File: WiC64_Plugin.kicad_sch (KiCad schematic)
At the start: 63 parts, among them CN1 PLUS4_USERPORT, CN2 OLED0.96, Q1 BSS138, Q10 BSS138, Q11 BSS138, Q2 BSS138, Q3 BSS138, Q4 BSS138, Q5 BSS138, Q6 BSS138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

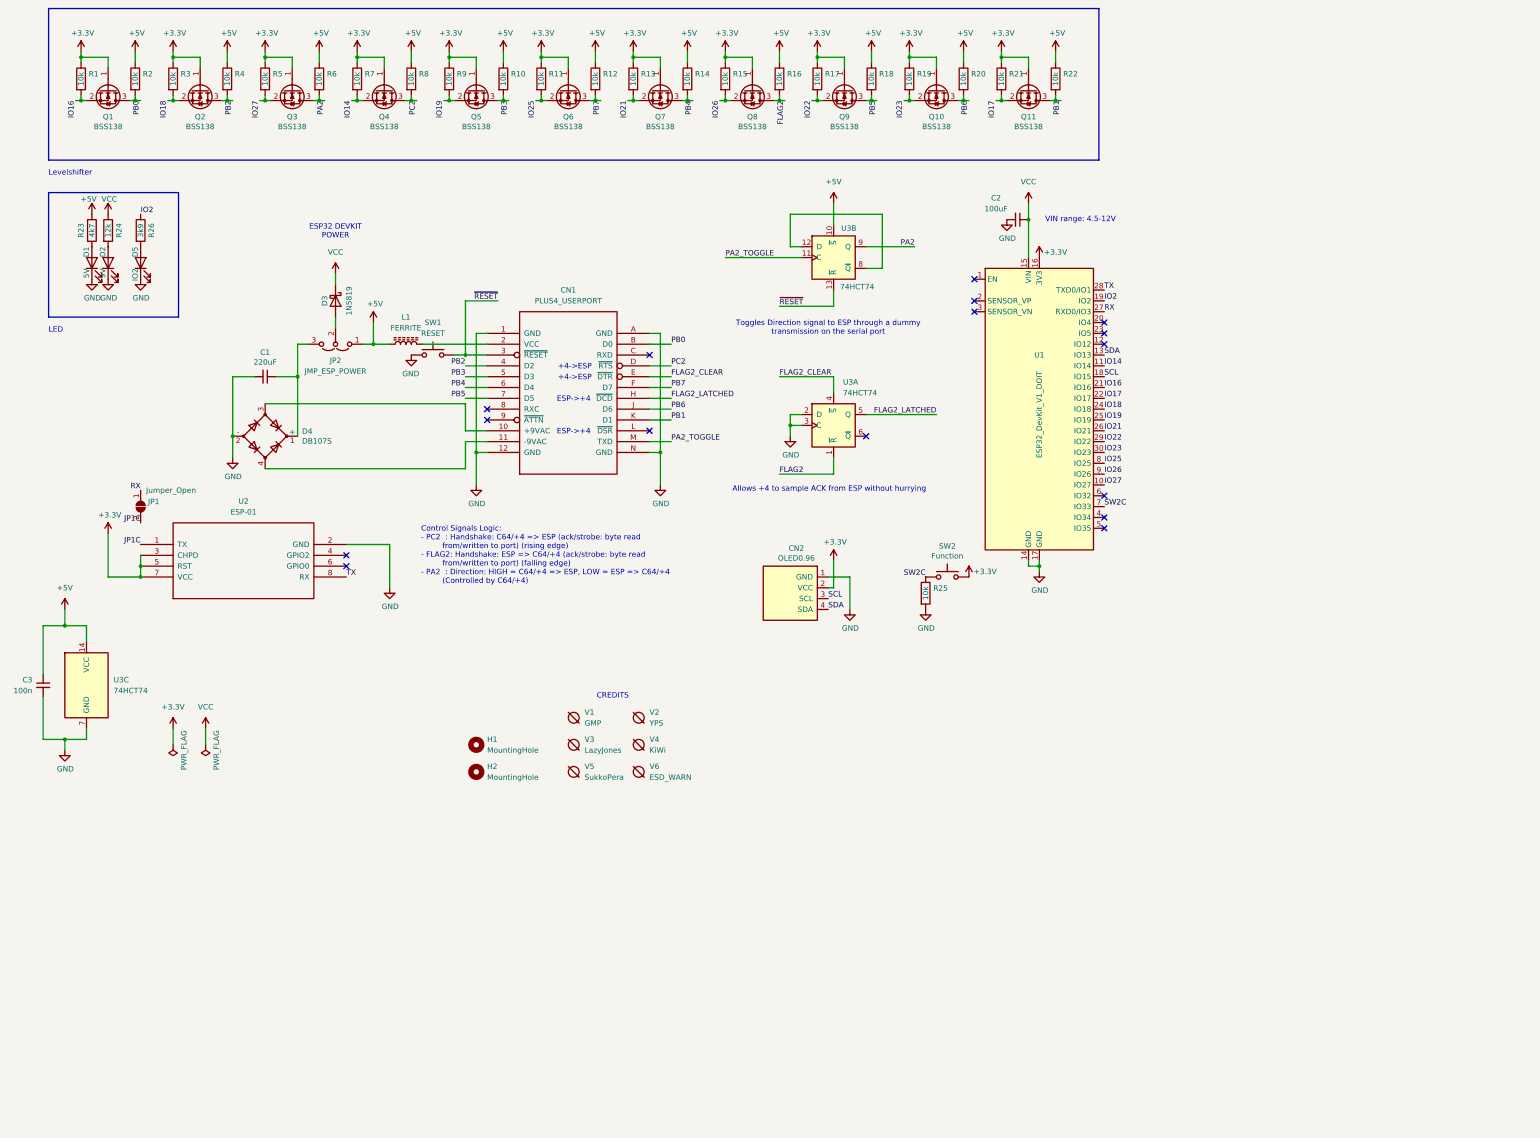
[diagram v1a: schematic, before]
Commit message: Add Schmitt trigger to clean TX signal
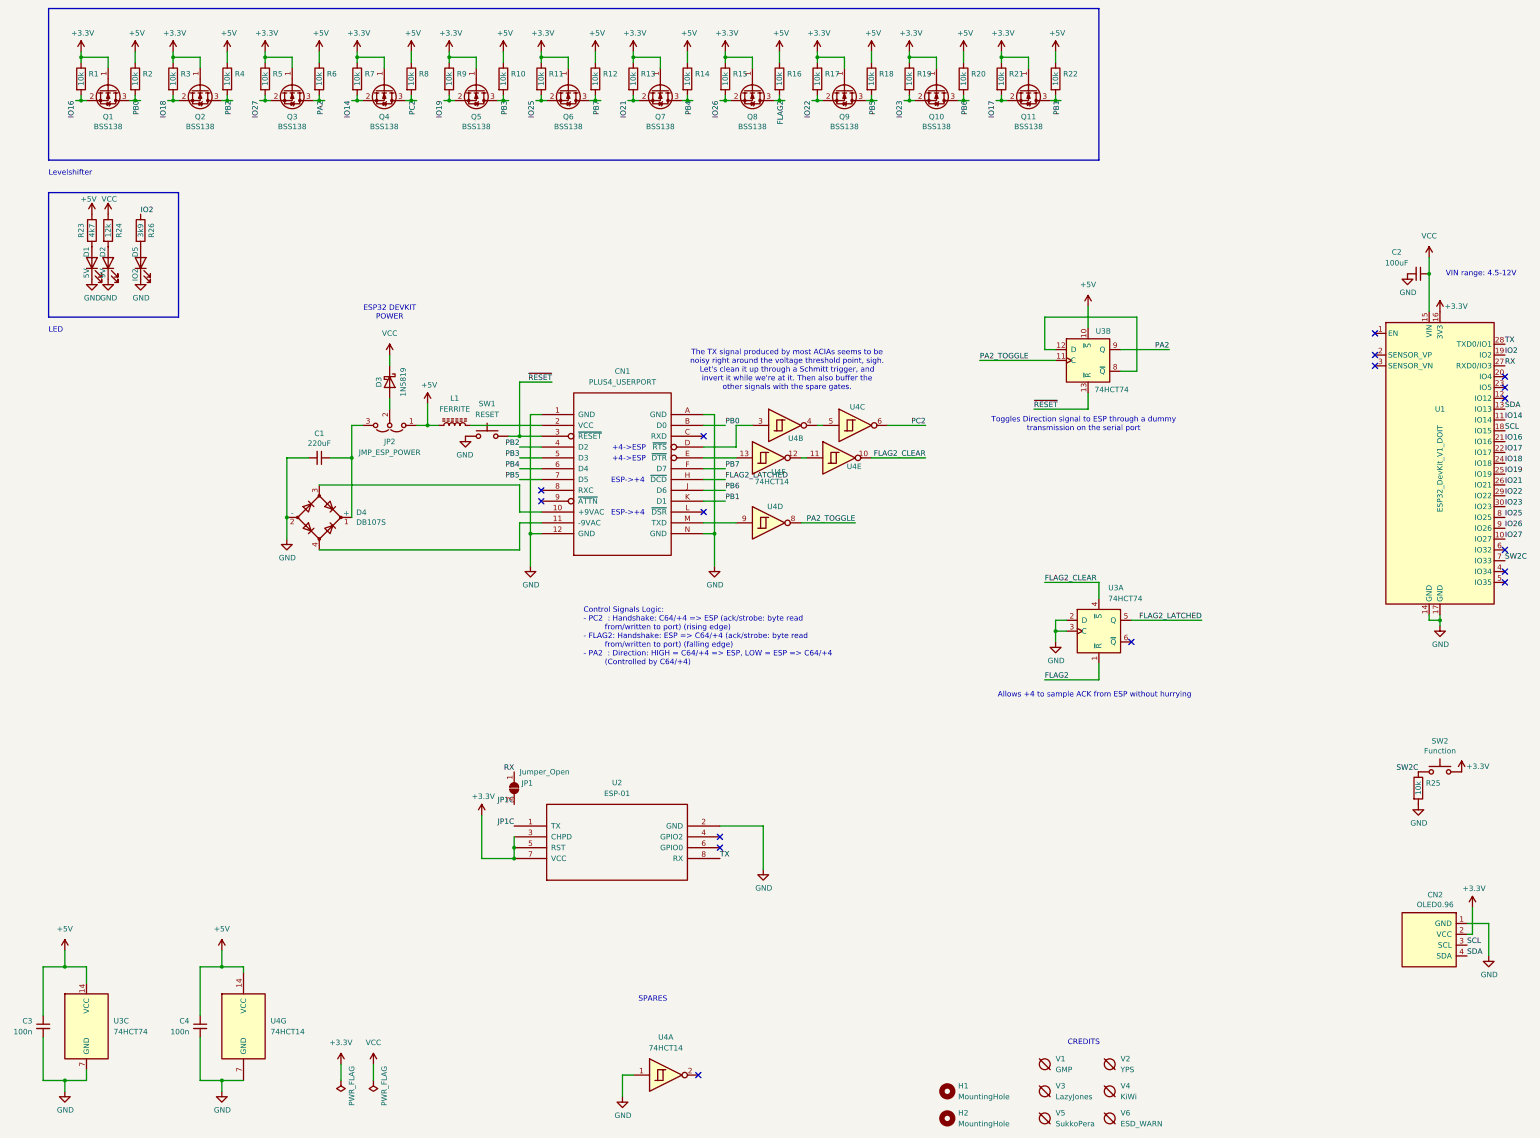
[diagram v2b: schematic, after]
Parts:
- added C4: 100n, Capacitor_SMD:C_0805_2012Metric_Pad1.18x1.45mm_HandSolder, symbol Device:C_Small
- added U4: 74HCT14, Package_SO:SOIC-14_3.9x8.7mm_P1.27mm, symbol 74xx:74LS14
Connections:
- net +5V: now also C4.1, U4.14 (VCC)
- net FLAG2_CLEAR: now also U4.10; no longer CN1.E (~{DTR})
- net GND: now also C4.2, U4.1, U4.7 (GND)
- net PA2_TOGGLE: now also U4.8; no longer CN1.M (TXD)
- net PC2: now also U4.6; no longer CN1.D (~{RTS})
- new net: CN1.M (TXD), U4.9
- new net: U4.11, U4.12
- new net: CN1.E (~{DTR}), U4.13
- new net: U4.4, U4.5
- new net: CN1.D (~{RTS}), U4.3
- no-connect marks 16 -> 17
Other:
- note added: "SPARES"
- note added: "The TX signal produced by most ACIAs seems to be noisy right around the voltage threshold point, sigh. Let's clean it up through a Schmitt trigger, and invert it while we're at it. Then also buffer the other signals with the spare gates."
- moved on the sheet: C1, C2, C3, CN1, CN2, D3, D4, H1, H2, JP1, JP2, L1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

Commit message: Various refinements for V1FFF
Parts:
- C1: value 220uF -> 220u; LCSC C269997 -> (C269997)
- C2: value 100uF -> 220u; LCSC C106598 -> (C269997)
- C3, C4: LCSC C269997 -> C49678
- CN2: LCSC (none) -> (C2718488)
- D1: LCSC C568936 -> (C568936)
- D2: LCSC C568937 -> (C568937)
- D3: footprint Diode_SMD:D_SOD-123 -> Diode_SMD:D_SMA; LCSC C402219 -> C8678
- D5: LCSC C331056 -> (C331056)
- H1, H2, JP1, JP2, V1, V2, V3, V4, V5, V6: LCSC (none) -> -
- Q1, Q10, Q11, Q2, Q3, Q4, Q5, Q6, Q7, Q8, Q9: footprint Package_TO_SOT_SMD:SOT-23 -> WiC64:SOT-23_Handsolder
- R1, R10, R11, R12, R13, R14, R15, R16, R17, R18, R19, R2, R20, R21, R22, R3, R4, R5, R6, R7, R8, R9: value 10k -> 1k; LCSC C25804 -> C17513
- R23: value 4k7 -> 680; LCSC C23162 -> C17798
- R24: value 12k -> 680; LCSC C22790 -> C17798
- R25: LCSC C25804 -> C17414
- R26: value 3k9 -> 220; LCSC C23018 -> C17557
- SW1: value RESET -> BTN_RESET; LCSC C406160 -> (C406160)
- SW2: value Function -> BTN_FUNCTION; LCSC C406160 -> (C406160)
- U1: LCSC (none) -> (C7509525)
- U2: LCSC (none) -> (C2977588); now not fitted
- U3: LCSC (none) -> C39990
- U4: LCSC (none) -> C609750
